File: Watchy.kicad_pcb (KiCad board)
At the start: 2 copper layers, 33.8 x 46 mm, 67 parts, among them J1 FPC24(0.5MM), J2 USB_C_Receptacle_USB2.0, J3 Battery, M1 Vibration_Motor, Q1 AO3400A, Q2 UMH3N, Q4 CJ2301, Q5 S8050, SW1 BTN, SW2 BTN, SW3 BTN, SW4 BTN, U1 ESP32-PICO-D4, U2 ME6211C33M5G-N, U3 CP2102, U4 BMA423, U5 TP4054, U6 PCF8563BS, Y1 32.768KHz

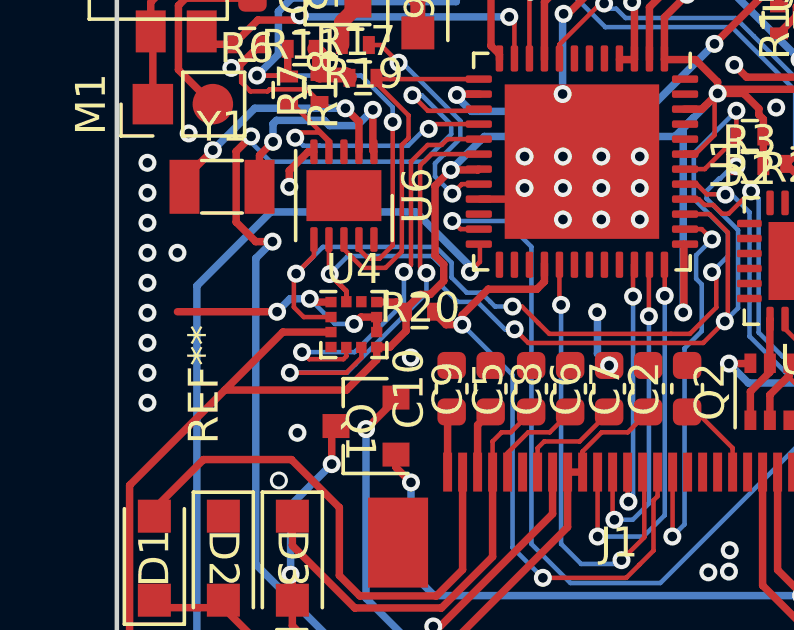
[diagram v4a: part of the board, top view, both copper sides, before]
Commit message: remove watchy and sqfmi on mask
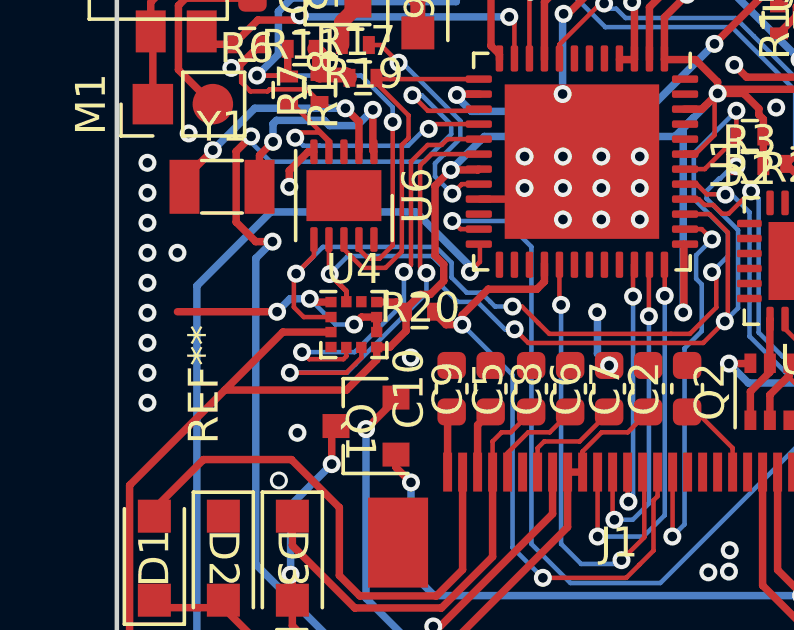
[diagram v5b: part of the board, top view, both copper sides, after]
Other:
- board text removed: "SQFMI"
- board text removed: "watchy"
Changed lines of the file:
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@@
     (effects (font (size 1 1) (thickness 0.15)) (justify mirror))
-  )
-  (gr_text "watchy" (at 94.935 125.6208) (layer "B.Mask")
-    (effects (font (size 1 1) (thickness 0.25)) (justify mirror))
-  )
-  (gr_text "watchy" (at 88.135 122.4408 180) (layer "B.Mask")
-    (effects (font (size 1 0.9) (thickness 0.15)) (justify mirror))
-  )
-  (gr_text "watchy" (at 92.12 99.66) (layer "B.Mask")
-    (effects (font (size 1 0.9) (thickness 0.15)) (justify mirror))
-  )
-  (gr_text "watchy" (at 98.6 98.93) (layer "B.Mask")
-    (effects (font (size 1 0.9) (thickness 0.15)) (justify mirror))
-  )
-  (gr_text "watchy" (at 86.34 109.41) (layer "B.Mask")
-    (effects (font (size 1 0.9) (thickness 0.15)) (justify mirror))
-  )
-  (gr_text "watchy" (at 74.6 110.04) (layer "B.Mask")
-    (effects (font (size 1 0.9) (thickness 0.15) italic) (justify mirror))
-  )
-  (gr_text "watchy" (at 73.95 103.27) (layer "B.Mask")
-    (effects (font (size 1 0.9) (thickness 0.15)) (justify mirror))
-  )
-  (gr_text "watchy" (at 78.66 99.73 45) (layer "B.Mask")
-    (effects (font (size 2 0.9) (thickness 0.15)) (justify mirror))
-  )
-  (gr_text "watchy" (at 73.91 98.59 180) (layer "B.Mask")
-    (effects (font (size 1 0.9) (thickness 0.15)) (justify mirror))
-  )
-  (gr_text "watchy" (at 75.93 90.44) (layer "B.Mask")
-    (effects (font (size 1 0.9) (thickness 0.15)) (justify mirror))
-  )
-  (gr_text "watchy" (at 82.27 95.62 315) (layer "B.Mask")
-    (effects (font (size 1 0.9) (thickness 0.15)) (justify mirror))
-  )
-  (gr_text "watchy" (at 97.76 81.24 -45) (layer "B.Mask")
-    (effects (font (size 0.75 0.75) (thickness 0.1)) (justify mirror))
-  )
-  (gr_text "watchy" (at 101.01 93.71 270) (layer "B.Mask")
-    (effects (font (size 1 0.9) (thickness 0.15)) (justify mirror))
   )
   (gr_text "WATCHY" (at 85.6 71.23) (layer "B.Mask")
@@
     (effects (font (size 1.3 1.3) (thickness 0.3)) (justify mirror))
   )
-  (gr_text "SQFMI" (at 95.9588 101.9362) (layer "F.Mask")
-    (effects (font (size 0.5 0.5) (thickness 0.125)))
-  )
   (gr_text "WATCHY" (at 85.6 115.18) (layer "F.Mask")
     (effects (font (size 1.3 1.3) (thickness 0.3)))
   )
-  (gr_text "watchy" (at 70.68 94.55 90) (layer "F.Mask")
-    (effects (font (size 1 0.9) (thickness 0.15)))
-  )
   (gr_text "WATCHY" (at 85.6 71.23) (layer "F.Mask")
     (effects (font (size 1.3 1.3) (thickness 0.3)))
@@
   (segment (start 72.845 83.808) (end 73.4934 83.1596) (width 0.1524) (layer "F.Cu") (net 1))
   (segment (start 93.026 102.0826) (end 93.026 103.0986) (width 0.25) (layer "F.Cu") (net 1))
-  (segment (start 77.3624 92.2528) (end 76.835 92.2528) (width 0.25) (layer "F.Cu") (net 1))
   (segment (start 96.87 87.862) (end 97.272 87.46) (width 0.5) (layer "F.Cu") (net 1))
   (segment (start 74.4474 87.3705) (end 74.4474 87.9094) (width 0.25) (layer "F.Cu") (net 1))
@@
   (segment (start 96.055 97.925) (end 95.69 97.56) (width 0.25) (layer "F.Cu") (net 1))
   (segment (start 73.7236 84.7296) (end 73.154646 84.7296) (width 0.1524) (layer "F.Cu") (net 1))
-  (segment (start 76.835 92.2528) (end 76.6064 92.4814) (width 0.25) (layer "F.Cu") (net 1))
   (segment (start 83.225 98.81296) (end 79.47276 102.5652) (width 0.25) (layer "F.Cu") (net 1))
   (segment (start 97.57872 104.2) (end 98.57872 105.2) (width 0.25) (layer "F.Cu") (net 1))
@@
   (segment (start 94.742 97.536) (end 94.742 98.907476) (width 0.5) (layer "F.Cu") (net 1))
   (segment (start 95.8596 85.6996) (end 95.5294 85.3694) (width 0.25) (layer "F.Cu") (net 1))
+  (segment (start 76.6064 92.5) (end 76.8536 92.2528) (width 0.25) (layer "F.Cu") (net 1))
   (segment (start 99.845 105.2) (end 100.72 106.075) (width 0.25) (layer "F.Cu") (net 1))
   (segment (start 83.740901 82.1436) (end 83.5914 82.1436) (width 0.25) (layer "F.Cu") (net 1))
@@
   (segment (start 91.1496 105.075) (end 90.72 105.075) (width 0.25) (layer "F.Cu") (net 1))
   (segment (start 97.029594 97.925) (end 96.055 97.925) (width 0.25) (layer "F.Cu") (net 1))
+  (segment (start 76.8536 92.2528) (end 77.3624 92.2528) (width 0.25) (layer "F.Cu") (net 1))
   (segment (start 81.91965 88.32035) (end 82.29 87.95) (width 0.25) (layer "F.Cu") (net 1))
   (segment (start 91.35 81.9034) (end 91.35 82.2194) (width 0.25) (layer "F.Cu") (net 1))
@@
   (via (at 69.72 92.11) (size 0.6) (drill 0.32) (layers "F.Cu" "B.Cu") (free) (net 1))
   (via (at 86.72 103.11) (size 0.6) (drill 0.32) (layers "F.Cu" "B.Cu") (free) (net 1))
-  (via (at 76.6064 92.4814) (size 0.6) (drill 0.32) (layers "F.Cu" "B.Cu") (net 1))
+  (via (at 76.6064 92.5) (size 0.6) (drill 0.32) (layers "F.Cu" "B.Cu") (net 1))
   (via (at 83.72 103.11) (size 0.6) (drill 0.32) (layers "F.Cu" "B.Cu") (free) (net 1))
   (via (at 84.72 110.11) (size 0.6) (drill 0.32) (layers "F.Cu" "B.Cu") (free) (net 1))
@@
   (via (at 88.72 103.11) (size 0.6) (drill 0.32) (layers "F.Cu" "B.Cu") (free) (net 1))
   (segment (start 75.1281 91.6432) (end 74.4728 91.6432) (width 0.25) (layer "B.Cu") (net 1))
-  (segment (start 75.1281 91.6432) (end 75.9663 92.4814) (width 0.1524) (layer "B.Cu") (net 1))
+  (segment (start 76.6064 92.5) (end 75.9849 92.5) (width 0.1524) (layer "B.Cu") (net 1))
   (segment (start 95.69 92.137233) (end 97.4714 93.918633) (width 0.25) (layer "B.Cu") (net 1))
   (segment (start 97.4714 95.2638) (end 97.2566 95.4786) (width 0.25) (layer "B.Cu") (net 1))
@@
   (segment (start 97.4714 93.918633) (end 97.4714 95.2638) (width 0.25) (layer "B.Cu") (net 1))
   (segment (start 78.6042 79.9592) (end 79.72 81.075) (width 0.25) (layer "B.Cu") (net 1))
+  (segment (start 75.9849 92.5) (end 75.1281 91.6432) (width 0.1524) (layer "B.Cu") (net 1))
   (segment (start 84.71 92.09) (end 84.72 92.1) (width 0.25) (layer "B.Cu") (net 1))
   (segment (start 84.72 92.08) (end 84.71 92.09) (width 0.25) (layer "B.Cu") (net 1))
   (segment (start 84.72 93.475) (end 85.11 93.865) (width 0.25) (layer "B.Cu") (net 1))
-  (segment (start 75.9663 92.4814) (end 76.6064 92.4814) (width 0.1524) (layer "B.Cu") (net 1))
   (segment (start 95.69 91.16) (end 95.69 92.137233) (width 0.25) (layer "B.Cu") (net 1))
   (segment (start 93.747 97.536) (end 92.985 96.774) (width 0.25) (layer "B.Cu") (net 1))

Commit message: change r location
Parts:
- moved R8 7.43 mm to (92.8, 109.5), turned to -90 degrees
- moved R9 6.47 mm to (91.7, 109.5), turned to 90 degrees
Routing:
- net GDR: track 22.7 -> 30.0 mm
- net RESE: track 30.0 -> 34.2 mm
- net GND: track 82.7 -> 79.0 mm, vias 148 -> 103

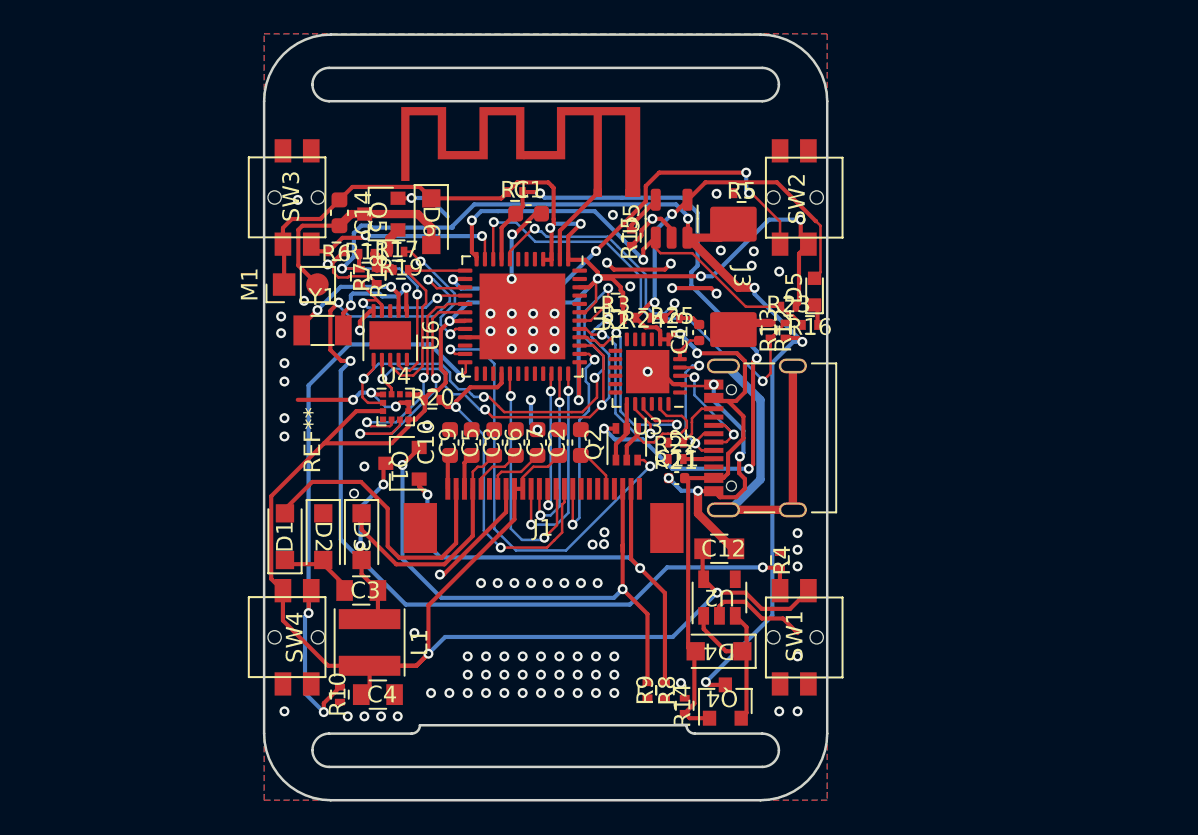
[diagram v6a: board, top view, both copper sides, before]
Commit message: small fixes
replaced quarz
fix button pads
mounting on display connector is ground
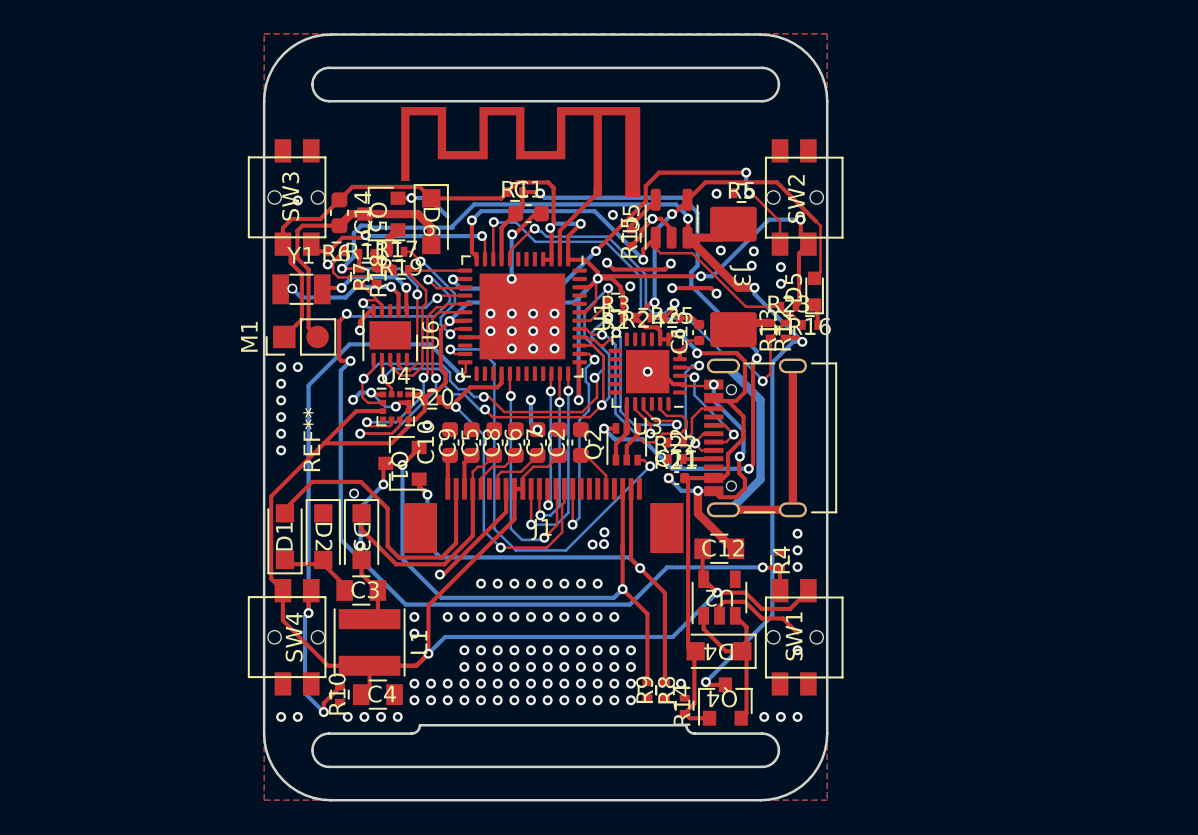
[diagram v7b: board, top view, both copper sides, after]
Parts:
- AE1: value SWRA117D -> Val**
- moved M1 3.15 mm to (69.9, 88.3)
- moved Y1 2.77 mm to (70.9, 85.4)
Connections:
- J1 pad M: (no net) -> GND
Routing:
- net +3V3: track 172.2 -> 176.2 mm
- net GND: track 79.0 -> 75.7 mm, vias 103 -> 138
- net Net-(D6-A): track 13.5 -> 16.7 mm
- net BTN_1: track 57.9 -> 56.1 mm
- net Net-(U6-OSCO): track 8.24 -> 8.77 mm

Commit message: fixes and improvements
- move battery pads
- fix battery footprint
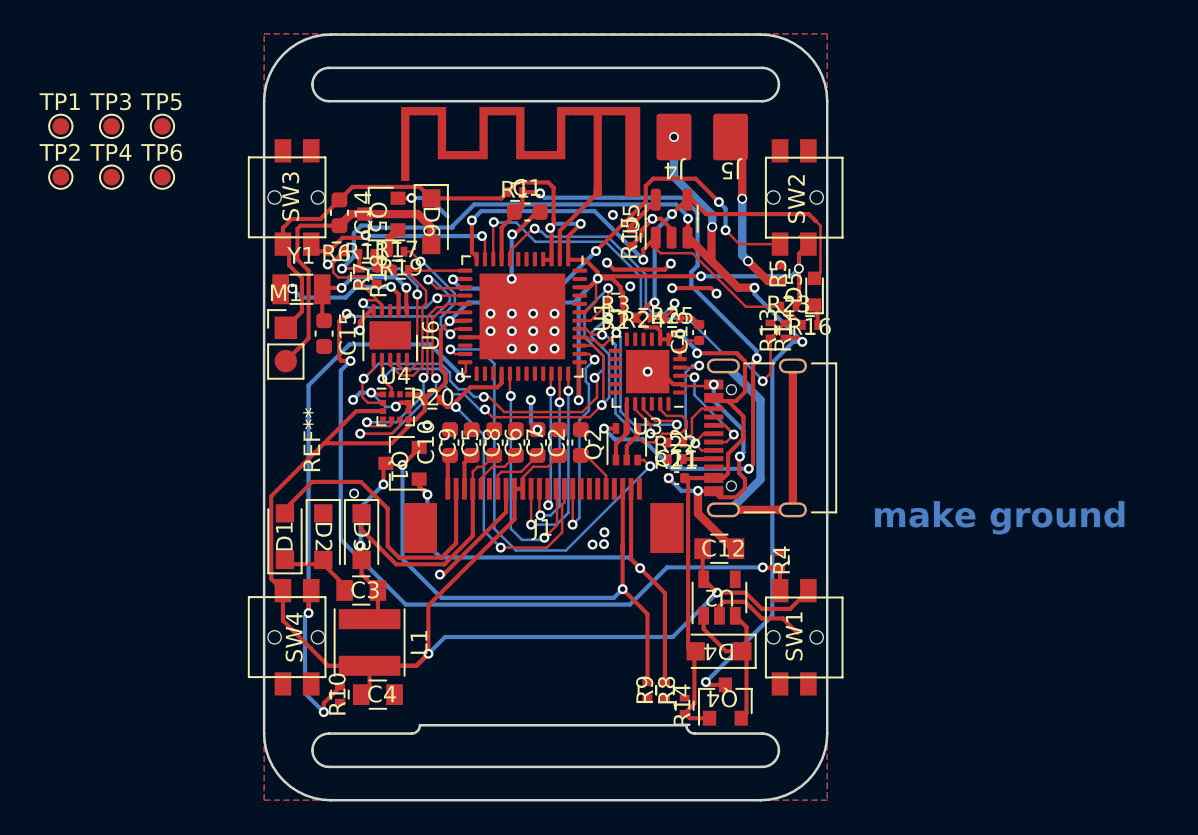
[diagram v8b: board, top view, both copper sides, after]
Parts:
- removed J3: Battery, Watchy:BatteryPads
- added C15: 22pF, Capacitor_SMD:C_0603_1608Metric, F.Cu at (72.3, 88.1)
- added J4: Conn_01x01, Watchy:BatteryPads, F.Cu at (93.3, 76.3)
- added J5: Conn_01x01, Watchy:BatteryPads, F.Cu at (96.7, 76.3)
- added TP1: GPIO0, TestPoint:TestPoint_Pad_D1.0mm, F.Cu at (56.5, 75.7)
- added TP2: SCL, TestPoint:TestPoint_Pad_D1.0mm, F.Cu at (56.5, 78.7)
- added TP3: SDA, TestPoint:TestPoint_Pad_D1.0mm, F.Cu at (59.5, 75.7)
- added TP4: 3V3, TestPoint:TestPoint_Pad_D1.0mm, F.Cu at (59.5, 78.7)
- added TP5: GND, TestPoint:TestPoint_Pad_D1.0mm, F.Cu at (62.6, 75.7)
- added TP6: GND, TestPoint:TestPoint_Pad_D1.0mm, F.Cu at (62.6, 78.7)
- AE1: value Val** -> SWRA117D
- C1: value 100nF -> 1uF/50V
- moved R5 5.37 mm to (99.7, 84.5), turned to 90 degrees
- moved M1 0.56 mm to (70.0, 87.8), turned to 0 degrees
- moved C1 0.12 mm to (84.5, 80.8)
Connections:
- J1 pad M: GND -> (no net)
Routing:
- net GND: track 75.7 -> 82.5 mm, vias 138 -> 41
- net +BATT: track 76.6 -> 81.9 mm, vias 6 -> 8
- net +3V3: track 176.2 -> 173.3 mm
- net Net-(U6-OSCI): track 7.01 -> 8.94 mm
- net Net-(D6-A): track 16.7 -> 18.6 mm
- net BTN_2: track 27.3 -> 26.3 mm
- net VBUS: track 58.4 -> 57.5 mm
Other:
- board text added: "make ground"
